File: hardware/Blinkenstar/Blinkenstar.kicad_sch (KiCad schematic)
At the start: 22 parts, among them SW1 SWITCH-4POMRON-6-6-SWITCH, SW2 SWITCH-4POMRON-6-6-SWITCH, U2 EEPROM-I2CEIAJ

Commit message: WIP
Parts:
- removed D1, D2: 1N4148, blinkenrocket_cr2032:SOD3718X135N, symbol blinkenrocket_cr2032-eagle-import:DIODE_SOD-123
- removed JP1: AUDIO-JACKPTH, blinkenrocket_cr2032:AUDIO-JACK, symbol blinkenrocket_cr2032-eagle-import:AUDIO-JACKPTH
- removed R4, R5, R6: 10K, blinkenrocket_cr2032:R1206, symbol blinkenrocket_cr2032-eagle-import:R-EU_R1206
- removed SW1, SW2: SWITCH-4POMRON-6-6-SWITCH, blinkenrocket_cr2032:4P-OMRON-6-6-SWITCH, symbol blinkenrocket_cr2032-eagle-import:SWITCH-4POMRON-6-6-SWITCH
- removed U$1: 2032, blinkenrocket_cr2032:KZH20SMD, symbol blinkenrocket_cr2032-eagle-import:2032
- removed U$2: U1, blinkenrocket_cr2032:TQFP32-08, symbol blinkenrocket_cr2032-eagle-import:TINY48/88B
- removed U$3: BATTERYPAD, blinkenrocket_cr2032:BATTERYPAD, symbol blinkenrocket_cr2032-eagle-import:BATTERYPAD
- removed U2: EEPROM-I2CEIAJ, blinkenrocket_cr2032:SO08-EIAJ, symbol blinkenrocket_cr2032-eagle-import:EEPROM-I2CEIAJ
- added BT1: Battery_Cell, Library:CR2032PAC_ELECTRODRAGON, symbol Device:Battery_Cell
- added D1, D2: 1N4148W, Diode_SMD:D_SOD-123, symbol Diode:1N4148W
- added J1: AudioJack2_Ground, Library:AUDIO-JACK, symbol Connector_Audio:AudioJack2_Ground
- added R4, R5, R6: 10K, Resistor_SMD:R_0603_1608Metric_Pad0.98x0.95mm_HandSolder, symbol Device:R
- added S1, S2: B3F-1000, Library:B3F-10XX, symbol B3F-1000:B3F-1000
- added U2: ATtiny88-A, Package_QFP:TQFP-32_7x7mm_P0.8mm, symbol MCU_Microchip_ATtiny:ATtiny88-A
- added U3: EEPROM-I2CEIAJ, Package_SO:SOIC-8_3.9x4.9mm_P1.27mm, symbol Memory_EEPROM:AT24CS01-SSHM
- C1, C2, C3: footprint blinkenrocket_cr2032:C1206 -> Capacitor_SMD:C_0603_1608Metric_Pad1.08x0.95mm_HandSolder
- ISP1: renamed from ISP0; footprint blinkenrocket_cr2032:AVR-ISP-6 -> Connector_PinHeader_2.54mm:PinHeader_2x03_P2.54mm_Vertical
- JP1: renamed from JP3; footprint blinkenrocket_cr2032:1X04-S -> Connector_PinHeader_1.00mm:PinHeader_1x04_P1.00mm_Vertical
- JP2: renamed from JP4; footprint blinkenrocket_cr2032:1X04-S -> Connector_PinHeader_1.00mm:PinHeader_1x04_P1.00mm_Vertical
- LED1: footprint blinkenrocket_cr2032:SEGMENT_BL-M12A881UR -> Library:SEGMENT_BL-M12A883
- R1: renamed from R3; footprint blinkenrocket_cr2032:R1206 -> Resistor_SMD:R_0603_1608Metric_Pad0.98x0.95mm_HandSolder
- R2: renamed from R1; footprint blinkenrocket_cr2032:R1206 -> Resistor_SMD:R_0603_1608Metric_Pad0.98x0.95mm_HandSolder
- R3: renamed from R2; footprint blinkenrocket_cr2032:R1206 -> Resistor_SMD:R_0603_1608Metric_Pad0.98x0.95mm_HandSolder
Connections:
- net AVR_AUDIO_IN: now also U2.19 (PA0)
- net B1: now also S1.1, U2.20 (PC7)
- net B2: now also S2.1, U2.26 (PC3)
- net C1: now also U2.30 (PD0)
- net C2: now also U2.31 (PD1)
- net C3: now also U2.32 (PD2)
- net C4: now also U2.1 (PD3)
- net C5: now also U2.2 (PD4)
- net C6: now also U2.9 (PD5)
- net C7: now also U2.10 (PD6)
- net C8: now also U2.11 (PD7)
- net E1: now also U2.23 (PC0)
- net E2: now also U2.24 (PC1)
- net E3: now also U2.25 (PC2)
- net E4: now also U2.22 (PA1)
- net GND: now also BT1.2 (-), D1.1 (K), D2.2 (A), J1.G, S1.3, S2.3, U2.21 (GND), U2.5 (GND), U3.1 (A0), U3.2 (A1), U3.3 (A2), U3.4 (GND), U3.7 (WP)
- net R1: now also U2.12 (PB0)
- net R2: now also U2.13 (PB1)
- net R3: now also U2.14 (PB2)
- net R4/MOSI: now also U2.15 (PB3)
- net R5/MISO: now also U2.16 (PB4)
- net R6/SCK: now also U2.17 (PB5)
- net R7: now also U2.7 (PB6)
- net R8: now also U2.8 (PB7)
- net RESET: now also R4.1, U2.29 (~{RESET}/PC6)
- net SCL: now also R5.2, U2.28 (PC5), U3.6 (SCL)
- net SDA: now also R6.2, U2.27 (PC4), U3.5 (SDA)
- net TRIG1: now also U2.3 (PA2)
- net TRIG2: now also U2.6 (PA3)
- net VCC: now also BT1.1 (+), R4.2, R5.1, R6.1, U2.18 (AVCC), U2.4 (VCC), U3.8 (VCC)
- net at C1.1, R1.1: now also D1.2 (A), D2.1 (K)
- net at R1.2: now also J1.S
- no-connect marks 0 -> 1
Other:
- moved on the sheet: C3

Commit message: WIP
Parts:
- added CR1: TEPT5700, TEPT5700:LED_TEPT5700, symbol TEPT5700:TEPT5700
- added R7: 10K, Resistor_SMD:R_0603_1608Metric_Pad0.98x0.95mm_HandSolder, symbol Device:R
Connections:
- net GND: now also CR1.1
- net VCC: now also R7.1
- new net To ATtiny88 input pin (e.g., INT0): CR1.2, R7.2

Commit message: Adds CLKI connector for clock input
Adds a single-pin connector for external clock input (CLKI).

This enables the Blinkenstar to synchronize with an external clock source.

Also sets 'exclude_from_bom' and 'dnp' attributes to the test point components.
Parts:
- added J3: CLKI, Connector_PinHeader_2.54mm:PinHeader_1x01_P2.54mm_Vertical, symbol Connector:Conn_01x01_Pin
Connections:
- net R7 renamed R7/CLKI
- net R7/CLKI: now also J3.1 (Pin_1)
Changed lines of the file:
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@@
 	(wire
 		(pts
+			(xy 257.81 81.28) (xy 261.62 81.28)
+		)
+		(stroke
+			(width 0)
+			(type default)
+		)
+	)
+	(wire
+		(pts
 			(xy 233.68 107.95) (xy 238.76 107.95)
 		)
@@
 		)
 	)
+	(label "R7{slash}CLKI"
+		(at 261.62 81.28 0)
+		(effects
+			(font
+				(size 1.2446 1.2446)
+			)
+			(justify left bottom)
+		)
+	)
 	(label "R8"
 		(at 96.52 157.48 180)
@@
 		)
 	)
-	(label "R7"
+	(label "R7{slash}CLKI"
 		(at 275.59 170.18 0)
 		(effects
@@
 		)
 	)
-	(label "R7"
+	(label "R7{slash}CLKI"
 		(at 96.52 147.32 180)
 		(effects
@@
 					(unit 1)
 				)
+			)
+		)
+	)
+	(symbol
+		(lib_id "Connector:Conn_01x01_Pin")
+		(at 252.73 81.28 0)
+		(unit 1)
+		(exclude_from_sim no)
+		(in_bom yes)
+		(on_board yes)
+		(dnp no)
+		(fields_autoplaced yes)
+		(property "Reference" "J3"
+			(at 253.365 76.2 0)
+			(effects
+				(font
+					(size 1.27 1.27)
+				)
+			)
+		)
+		(property "Value" "CLKI"
+			(at 253.365 78.74 0)
+			(effects
+				(font
+					(size 1.27 1.27)
+				)
+			)
+		)
+		(property "Footprint" "Connector_PinHeader_2.54mm:PinHeader_1x01_P2.54mm_Vertical"
+			(at 252.73 81.28 0)
+			(effects
+				(font
+					(size 1.27 1.27)
+				)
+				(hide yes)
+			)
+		)
+		(property "Datasheet" "~"
+			(at 252.73 81.28 0)
+			(effects
+				(font
+					(size 1.27 1.27)
+				)
+				(hide yes)
+			)
+		)
+		(property "Description" "Generic connector, single row, 01x01, script generated"
+			(at 252.73 81.28 0)
+			(effects
+				(font
+					(size 1.27 1.27)
+				)
+				(hide yes)
+			)
+		)
+		(pin "1"
+		)
+		(instances
+			(project ""
+				(path "/aef0e59a-a546-4e07-b43f-b7b911a1cb8f"
+					(reference "J3")
+					(unit 1)
+				)

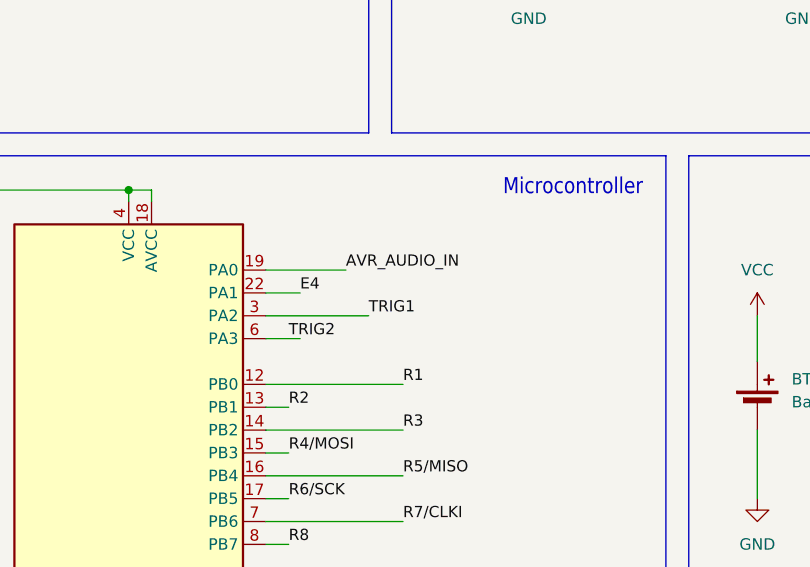
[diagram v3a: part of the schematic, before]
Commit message: feat: add audio output and sine wave generation functionality
- Implemented audio output capabilities with the Speaker module.
- Created functions for generating and playing sine wave PCM audio.
- Added transfer tone encoding and playback features.
- Developed tests for audio output, sine wave generation, and transfer tone encoding.
- Ensured all scripts are in ES module format and removed legacy .js files.
- Updated package.json to include new test scripts for audio functionalities.
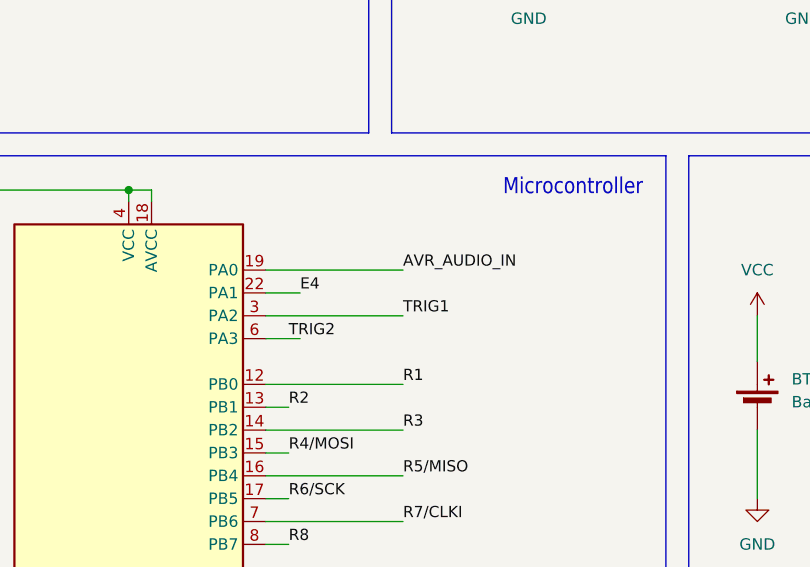
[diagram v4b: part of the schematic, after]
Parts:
- BT1: LCSC (none) -> C19184089
- C1: LCSC (none) -> C19702
- C2, C3: LCSC (none) -> C1623
- D1, D2: LCSC (none) -> C7420318
- J1: LCSC (none) -> C16684
- R1: LCSC (none) -> C217814
- R2: LCSC (none) -> C25981
- R3: LCSC (none) -> C23212
- R4, R5, R6: LCSC (none) -> C25804
- S1, S2: LCSC (none) -> C393938
- U2: LCSC (none) -> C111451
- U3: LCSC (none) -> C79988
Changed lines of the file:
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@@
 	(title_block
 		(title "Blinkenstar")
-		(date "2025-03-28")
-		(rev "2.7")
+		(date "2026-04-02")
+		(rev "2.8")
 		(company "Sternenlabor e.V.")
 		(comment 1 "André Fiedler <mail@andrefiedler.de>")
@@
 	(wire
 		(pts
-			(xy 260.35 147.32) (xy 271.78 147.32)
+			(xy 260.35 147.32) (xy 275.59 147.32)
 		)
 		(stroke
@@
 	(wire
 		(pts
-			(xy 260.35 142.24) (xy 269.24 142.24)
+			(xy 260.35 142.24) (xy 275.59 142.24)
 		)
 		(stroke
@@
 	)
 	(label "TRIG1"
-		(at 271.78 147.32 0)
+		(at 275.59 147.32 0)
 		(effects
 			(font
@@
 	)
 	(label "AVR_AUDIO_IN"
-		(at 269.24 142.24 0)
+		(at 275.59 142.24 0)
 		(effects
 			(font
@@
 			)
 		)
+		(property "LCSC" "C79988"
+			(at 209.55 107.95 0)
+			(effects
+				(font
+					(size 1.27 1.27)
+				)
+				(hide yes)
+			)
+		)
 		(pin "5"
 		)
@@
 			)
 		)
+		(property "LCSC" "C25804"
+			(at 233.68 101.6 90)
+			(effects
+				(font
+					(size 1.27 1.27)
+				)
+				(hide yes)
+			)
+		)
 		(pin "1"
 		)
@@
 			)
 		)
+		(property "LCSC" "C1623"
+			(at 205.74 154.94 0)
+			(effects
+				(font
+					(size 1.27 1.27)
+				)
+				(hide yes)
+			)
+		)
 		(pin "1"
 		)
@@
 			)
 		)
+		(property "LCSC" "C217814"
+			(at 106.68 195.58 0)
+			(effects
+				(font
+					(size 1.27 1.27)
+				)
+				(hide yes)
+			)
+		)
 		(pin "1"
 		)
@@
 			)
 		)
+		(property "LCSC" "C19184089"
+			(at 314.96 157.48 0)
+			(effects
+				(font
+					(size 1.27 1.27)
+				)
+				(hide yes)
+			)
+		)
 		(pin "2"
 		)
@@
 			)
 		)
+		(property "LCSC" "C7420318"
+			(at 114.3 204.47 0)
+			(effects
+				(font
+					(size 1.27 1.27)
+				)
+				(hide yes)
+			)
+		)
 		(pin "1"
 		)
@@
 			)
 		)
+		(property "LCSC" "C111451"
+			(at 245.11 180.34 0)
+			(effects
+				(font
+					(size 1.27 1.27)
+				)
+				(hide yes)
+			)
+		)
 		(pin "19"
 		)
@@
 			)
 		)
+		(property "LCSC" "C393938"
+			(at 303.53 66.04 0)
+			(effects
+				(font
+					(size 1.27 1.27)
+				)
+				(hide yes)
+			)
+		)
 		(pin "2"
 		)
@@
 			)
 		)
+		(property "LCSC" "C393938"
+			(at 303.53 43.18 0)
+			(effects
+				(font
+					(size 1.27 1.27)
+				)
+				(hide yes)
+			)
+		)
 		(pin "2"
 		)
@@
 			)
 		)
+		(property "LCSC" "C16684"
+			(at 91.44 198.12 0)
+			(effects
+				(font
+					(size 1.27 1.27)
+				)
+				(hide yes)
+			)
+		)
 		(pin "S"
 		)
@@
 			)
 		)
+		(property "LCSC" "C7420318"
+			(at 119.38 204.47 0)
+			(effects
+				(font
+					(size 1.27 1.27)
+				)
+				(hide yes)
+			)
+		)
 		(pin "1"
 		)
@@
 			)
 		)
+		(property "LCSC" "C25804"
+			(at 246.38 101.6 90)
+			(effects
+				(font
+					(size 1.27 1.27)
+				)
+				(hide yes)
+			)
+		)
 		(pin "1"
 		)
@@
 			)
 		)
+		(property "LCSC" "C19702"
+			(at 127 195.58 0)
+			(effects
+				(font
+					(size 1.27 1.27)
+				)
+				(hide yes)
+			)
+		)
 		(pin "1"
 		)
@@
 			)
 		)
+		(property "LCSC" "C23212"
+			(at 137.16 203.2 0)
+			(effects
+				(font
+					(size 1.27 1.27)
+				)
+				(hide yes)
+			)
+		)
 		(pin "1"
 		)
@@
 			)
 		)
+		(property "LCSC" "C25981"
+			(at 137.16 185.42 0)
+			(effects
+				(font
+					(size 1.27 1.27)
+				)
+				(hide yes)
+			)
+		)
 		(pin "1"
 		)
@@
 			)
 		)
+		(property "LCSC" "C1623"
+			(at 147.32 203.2 0)
+			(effects
+				(font
+					(size 1.27 1.27)
+				)
+				(hide yes)
+			)
+		)
 		(pin "1"
 		)
@@
 			(effects
 				(font
+					(size 1.27 1.27)
+				)
+				(hide yes)
+			)
+		)
+		(property "LCSC" "C25804"
+			(at 218.44 73.66 90)
+			(effects
+				(font

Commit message: feat: rename legacy identifiers to blinkenstar and update related tests
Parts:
- C1, C2, C3: symbol blinkenrocket_cr2032-eagle-import:C-EUC1206 -> blinkenstar_cr2032-eagle-import:C-EUC1206
- ISP1: symbol blinkenrocket_cr2032-eagle-import:AVR-ISP-6VERT -> blinkenstar_cr2032-eagle-import:AVR-ISP-6VERT
- JP1, JP2: symbol blinkenrocket_cr2032-eagle-import:PINHD-1X04_2.54-S -> blinkenstar_cr2032-eagle-import:PINHD-1X04_2.54-S
- LED1: symbol blinkenrocket_cr2032-eagle-import:SEGMENT_8X8_ROWCATHODEM12A881UR -> blinkenstar_cr2032-eagle-import:SEGMENT_8X8_ROWCATHODEM12A881UR
- R1, R2, R3: symbol blinkenrocket_cr2032-eagle-import:R-EU_R1206 -> blinkenstar_cr2032-eagle-import:R-EU_R1206
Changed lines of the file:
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@@
 	)
 	(symbol
-		(lib_id "blinkenrocket_cr2032-eagle-import:C-EUC1206")
+		(lib_id "blinkenstar_cr2032-eagle-import:C-EUC1206")
 		(at 205.74 154.94 0)
 		(unit 1)
@@
 	)
 	(symbol
-		(lib_id "blinkenrocket_cr2032-eagle-import:R-EU_R1206")
+		(lib_id "blinkenstar_cr2032-eagle-import:R-EU_R1206")
 		(at 106.68 195.58 0)
 		(mirror y)
@@
 	)
 	(symbol
-		(lib_id "blinkenrocket_cr2032-eagle-import:SEGMENT_8X8_ROWCATHODEM12A881UR")
+		(lib_id "blinkenstar_cr2032-eagle-import:SEGMENT_8X8_ROWCATHODEM12A881UR")
 		(at 142.24 119.38 0)
 		(unit 1)
@@
 	)
 	(symbol
-		(lib_id "blinkenrocket_cr2032-eagle-import:PINHD-1X04_2.54-S")
+		(lib_id "blinkenstar_cr2032-eagle-import:PINHD-1X04_2.54-S")
 		(at 307.34 106.68 0)
 		(mirror y)
@@
 	)
 	(symbol
-		(lib_id "blinkenrocket_cr2032-eagle-import:C-EUC1206")
+		(lib_id "blinkenstar_cr2032-eagle-import:C-EUC1206")
 		(at 127 195.58 90)
 		(unit 1)
@@
 	)
 	(symbol
-		(lib_id "blinkenrocket_cr2032-eagle-import:R-EU_R1206")
+		(lib_id "blinkenstar_cr2032-eagle-import:R-EU_R1206")
 		(at 137.16 203.2 90)
 		(unit 1)
@@
 	)
 	(symbol
-		(lib_id "blinkenrocket_cr2032-eagle-import:PINHD-1X04_2.54-S")
+		(lib_id "blinkenstar_cr2032-eagle-import:PINHD-1X04_2.54-S")
 		(at 302.26 106.68 0)
 		(unit 1)
@@
 	)
 	(symbol
-		(lib_id "blinkenrocket_cr2032-eagle-import:R-EU_R1206")
+		(lib_id "blinkenstar_cr2032-eagle-import:R-EU_R1206")
 		(at 137.16 185.42 90)
 		(unit 1)
@@
 	)
 	(symbol
-		(lib_id "blinkenrocket_cr2032-eagle-import:C-EUC1206")
+		(lib_id "blinkenstar_cr2032-eagle-import:C-EUC1206")
 		(at 147.32 203.2 0)
 		(unit 1)
@@
 	)
 	(symbol
-		(lib_id "blinkenrocket_cr2032-eagle-import:AVR-ISP-6VERT")
+		(lib_id "blinkenstar_cr2032-eagle-import:AVR-ISP-6VERT")
 		(at 228.6 66.04 0)
 		(unit 1)
